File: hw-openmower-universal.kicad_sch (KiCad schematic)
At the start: 51 parts

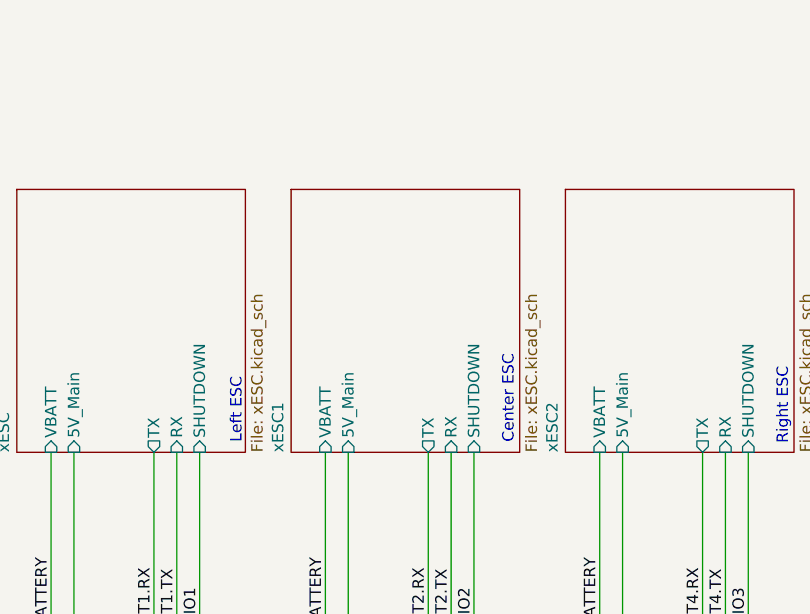
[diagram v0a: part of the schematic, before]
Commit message: New conns for xESC
Added new connectors into the design for motors.
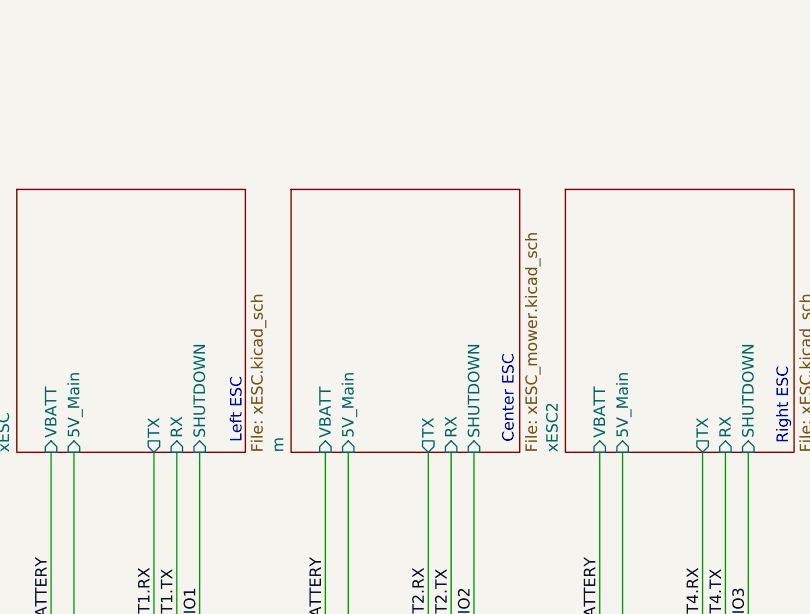
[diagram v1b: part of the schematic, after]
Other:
- sheet xESC1 renamed m
- sheet m: file xESC.kicad_sch -> xESC_mower.kicad_sch

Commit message: Routing progress and vertical USB
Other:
- sheet m renamed xESC_motor
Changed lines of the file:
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@@
 	(generator_version "9.0")
 	(paper "A3")
-	(rectangle
-		(start 429.26 8.89)
-		(end 857.25 279.4)
-		(stroke
-			(width 0)
-			(type default)
-		)
-		(fill
-			(type none)
-		)
-	)
 	(text "Left ESC"
 		(exclude_from_sim no)
@@
 			(color 0 0 0 0.0000)
 		)
-		(property "Sheetname" "m"
+		(property "Sheetname" "xESC_motor"
 			(at 144.0684 78.74 90)
 			(effects

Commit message: Incremental routing updates
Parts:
- removed U1, U48, U49, U61: ~, mousebites:Mousebite_4, symbol mousebites:Mousebite_4
- removed U2, U4, U50, U51, U52, U53, U54, U55, U56, U57, U58, U59, U60, U62, U63, U64, U65, U66, U67, U68, U69, U70, U71: ~, mousebites:Mousebite_8, symbol mousebites:Mousebite_8
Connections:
- no-connect marks 1 -> 0

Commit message: Routing progress
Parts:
- added B1: MouseBite, Panelization:MouseBite-Slot_2.0x2.0mm_outset_D0.5mm_P0.85mm_3h, symbol Mechanical:MouseBite
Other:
- sheet GPS ports: added none; removed 5V, RXD, TXD
- sheet subpcb_charger ports: added none; removed 5V, I2C{SDA SCL}, V_BATTERY, V_CHARGE_SENSE

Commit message: Further routing progress
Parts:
- removed H1, H14, H17, H2, H21, H22, H25, H26, H27, H28, H29, H3, H30, H31, H32, H7: MountingHole_Pad, MountingHole:MountingHole_4.3mm_M4_Pad_Via, symbol Mechanical:MountingHole_Pad

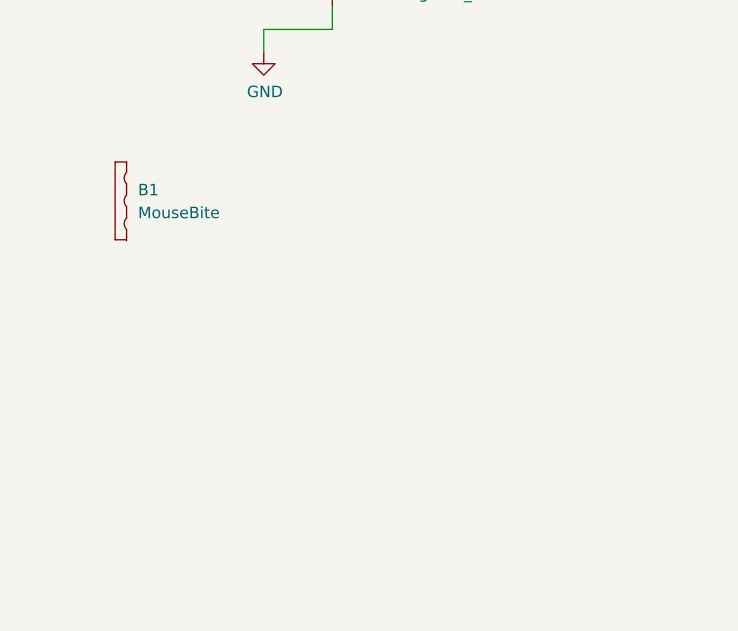
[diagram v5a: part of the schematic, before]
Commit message: Review ready layout
DRC mostly clean.  Need to add GND via stitching and GND return vias yet, and general review
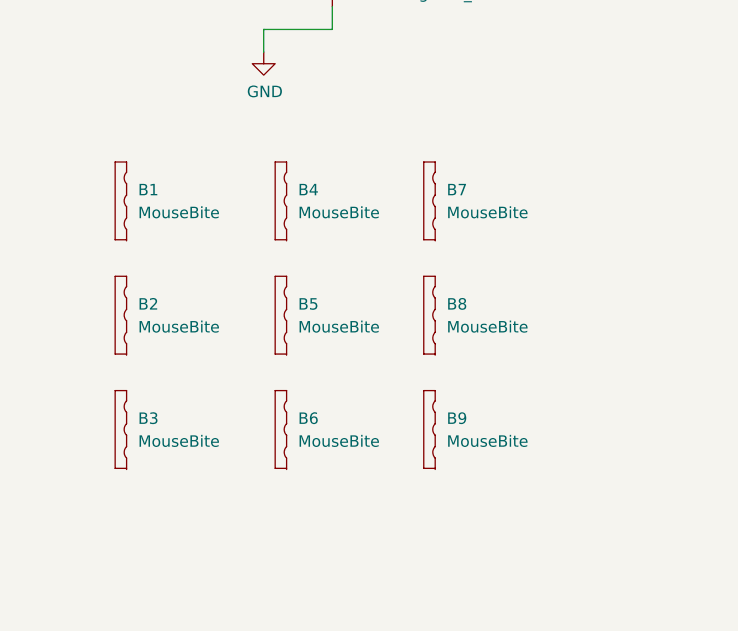
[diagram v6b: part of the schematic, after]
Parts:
- added B2, B3, B4, B5, B6, B7, B8, B9: MouseBite, Panelization:MouseBite-Slot_2.0x2.0mm_inset_D0.5mm_P0.85mm_4h_Trace, symbol Mechanical:MouseBite
- B1: footprint Panelization:MouseBite-Slot_2.0x2.0mm_outset_D0.5mm_P0.85mm_3h -> Panelization:MouseBite-Slot_2.0x2.0mm_inset_D0.5mm_P0.85mm_4h_Trace
